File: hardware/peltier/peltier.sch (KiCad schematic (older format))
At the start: 33 parts, among them J1 Conn_01x02, J2 Conn_01x04, J3 Conn_01x04, J5 Conn_01x02, J6 Conn_01x03, Q1 IRF9Z34NPBF, Q2 IRF9Z34NPBF, Q3 IRFZ24NPBF, Q4 IRFZ24NPBF, U1 TC4420CPA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

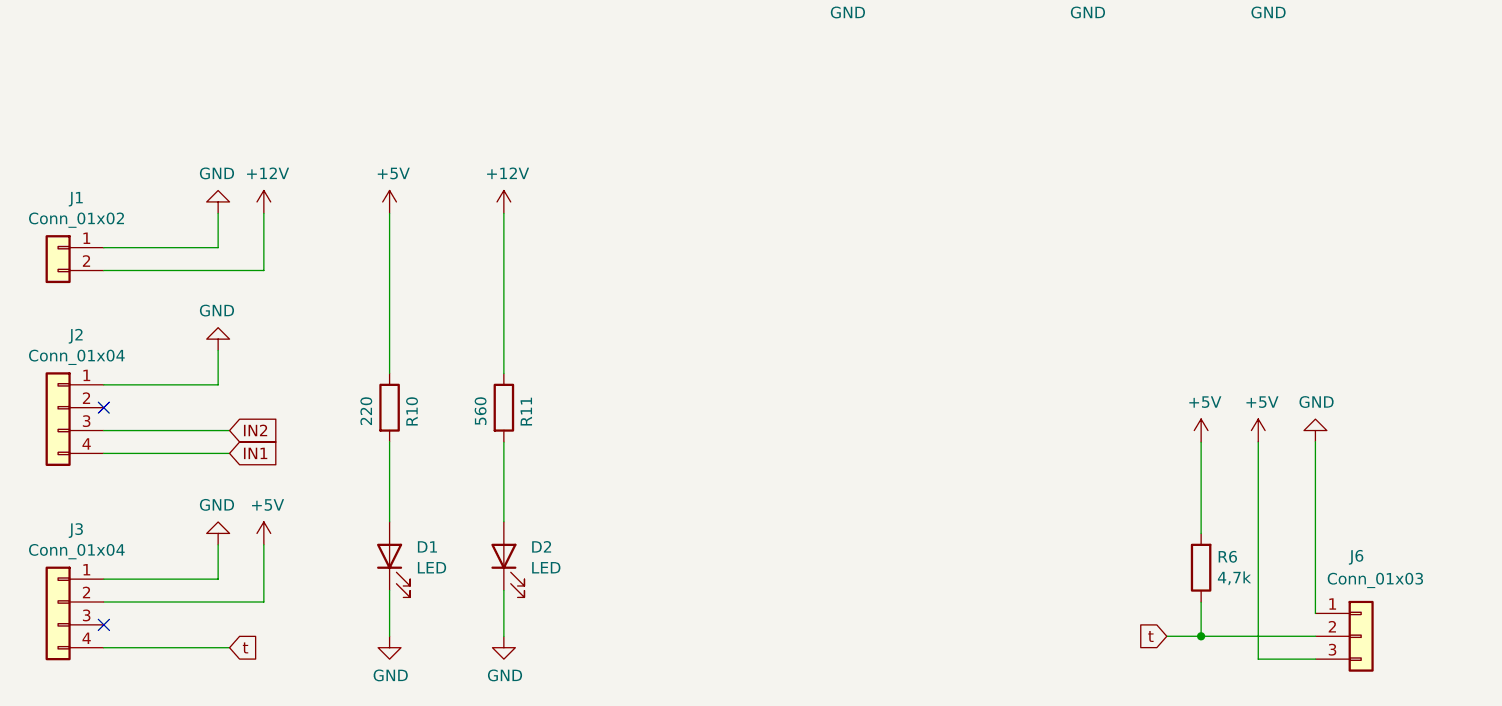
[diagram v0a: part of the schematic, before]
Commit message: Quick pinout fix for Peltier driver
Simple fix with  pinout now being correct
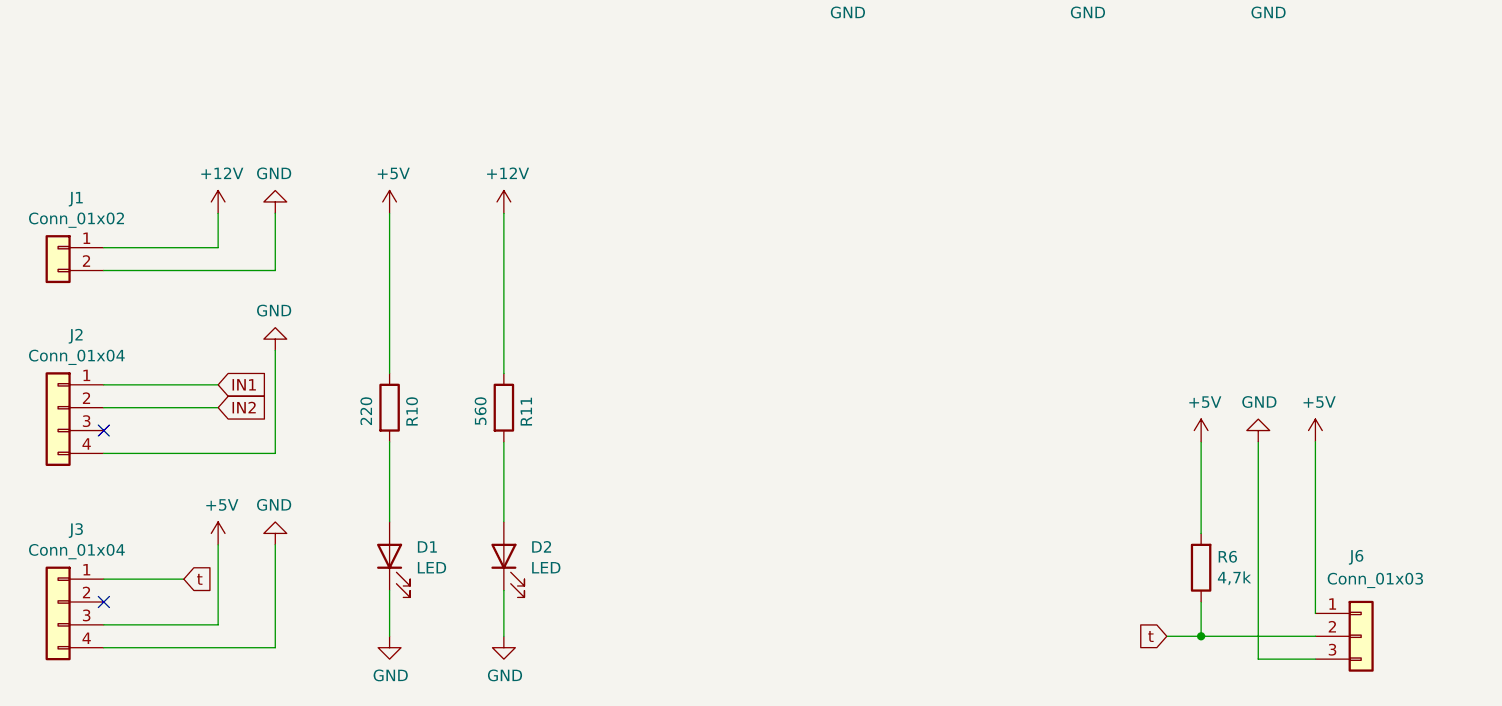
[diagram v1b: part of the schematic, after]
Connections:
- net +12V: now also J1.1 (Pin_1); no longer J1.2 (Pin_2)
- net +5V: now also J3.3 (Pin_3), J6.1 (Pin_1); no longer J3.2 (Pin_2), J6.3 (Pin_3)
- net GND: now also J1.2 (Pin_2), J2.4 (Pin_4), J3.4 (Pin_4), J6.3 (Pin_3); no longer J1.1 (Pin_1), J2.1 (Pin_1), J3.1 (Pin_1), J6.1 (Pin_1)
- net IN1: now also J2.1 (Pin_1); no longer J2.4 (Pin_4)
- net IN2: now also J2.2 (Pin_2); no longer J2.3 (Pin_3)
- net t: now also J3.1 (Pin_1); no longer J3.4 (Pin_4)
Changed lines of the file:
@@
 EESchema Schematic File Version 4
-LIBS:peltier-cache
 EELAYER 30 0
 EELAYER END
@@
 L power:GND #PWR022
 U 1 1 5F5A30FB
-P 6250 6650
-F 0 "#PWR022" H 6250 6400 50  0001 C CNN
-F 1 "GND" H 6255 6477 50  0000 C CNN
-F 2 "" H 6250 6650 50  0001 C CNN
-F 3 "" H 6250 6650 50  0001 C CNN
-	1    6250 6650
+P 6000 6650
+F 0 "#PWR022" H 6000 6400 50  0001 C CNN
+F 1 "GND" H 6005 6477 50  0000 C CNN
+F 2 "" H 6000 6650 50  0001 C CNN
+F 3 "" H 6000 6650 50  0001 C CNN
+	1    6000 6650
 	1    0    0    1
 $EndComp
@@
 L power:+5V #PWR021
 U 1 1 5F5B6024
-P 6000 6650
-F 0 "#PWR021" H 6000 6500 50  0001 C CNN
-F 1 "+5V" H 6015 6823 50  0000 C CNN
-F 2 "" H 6000 6650 50  0001 C CNN
-F 3 "" H 6000 6650 50  0001 C CNN
-	1    6000 6650
+P 6250 6650
+F 0 "#PWR021" H 6250 6500 50  0001 C CNN
+F 1 "+5V" H 6265 6823 50  0000 C CNN
+F 2 "" H 6250 6650 50  0001 C CNN
+F 3 "" H 6250 6650 50  0001 C CNN
+	1    6250 6650
 	1    0    0    -1
 $EndComp
@@
 L power:GND #PWR03
 U 1 1 5F58F426
-P 1450 6250
-F 0 "#PWR03" H 1450 6000 50  0001 C CNN
-F 1 "GND" H 1455 6077 50  0000 C CNN
-F 2 "" H 1450 6250 50  0001 C CNN
-F 3 "" H 1450 6250 50  0001 C CNN
-	1    1450 6250
+P 1700 6250
+F 0 "#PWR03" H 1700 6000 50  0001 C CNN
+F 1 "GND" H 1705 6077 50  0000 C CNN
+F 2 "" H 1700 6250 50  0001 C CNN
+F 3 "" H 1700 6250 50  0001 C CNN
+	1    1700 6250
 	-1   0    0    1
 $EndComp
@@
 L power:+5V #PWR08
 U 1 1 5F591312
-P 1650 7100
-F 0 "#PWR08" H 1650 6950 50  0001 C CNN
-F 1 "+5V" H 1665 7273 50  0000 C CNN
-F 2 "" H 1650 7100 50  0001 C CNN
-F 3 "" H 1650 7100 50  0001 C CNN
-	1    1650 7100
-	1    0    0    -1
-$EndComp
-Wire Wire Line
-	1500 6600 950  6600
+P 1450 7100
+F 0 "#PWR08" H 1450 6950 50  0001 C CNN
+F 1 "+5V" H 1465 7273 50  0000 C CNN
+F 2 "" H 1450 7100 50  0001 C CNN
+F 3 "" H 1450 7100 50  0001 C CNN
+	1    1450 7100
+	1    0    0    -1
+$EndComp
 $Comp
 L Connector_Generic:Conn_01x04 J3
@@
 L power:GND #PWR06
 U 1 1 5F59FAE5
-P 1450 7100
-F 0 "#PWR06" H 1450 6850 50  0001 C CNN
-F 1 "GND" H 1455 6927 50  0000 C CNN
-F 2 "" H 1450 7100 50  0001 C CNN
-F 3 "" H 1450 7100 50  0001 C CNN
-	1    1450 7100
+P 1700 7100
+F 0 "#PWR06" H 1700 6850 50  0001 C CNN
+F 1 "GND" H 1705 6927 50  0000 C CNN
+F 2 "" H 1700 7100 50  0001 C CNN
+F 3 "" H 1700 7100 50  0001 C CNN
+	1    1700 7100
 	-1   0    0    1
-$EndComp
-Wire Wire Line
-	1450 6400 1450 6250
-Wire Wire Line
-	1650 7100 1650 7350
-$Comp
-L Connector_Generic:Conn_01x02 J1
-U 1 1 5F5E0D51
-P 750 5800
-F 0 "J1" H 668 6017 50  0000 C CNN
-F 1 "Conn_01x02" H 668 5926 50  0000 C CNN
-F 2 "Connector_JST:JST_XH_B2B-XH-A_1x02_P2.50mm_Vertical" H 750 5800 50  0001 C CNN
-F 3 "~" H 750 5800 50  0001 C CNN
-	1    750  5800
-	-1   0    0    -1
 $EndComp
 $Comp
 L power:GND #PWR01
 U 1 1 5F5E28D2
+P 1700 5650
+F 0 "#PWR01" H 1700 5400 50  0001 C CNN
+F 1 "GND" H 1705 5477 50  0000 C CNN
+F 2 "" H 1700 5650 50  0001 C CNN
+F 3 "" H 1700 5650 50  0001 C CNN
+	1    1700 5650
+	-1   0    0    1
+$EndComp
+$Comp
+L power:+12V #PWR07
+U 1 1 5F5E4300
 P 1450 5650
-F 0 "#PWR01" H 1450 5400 50  0001 C CNN
-F 1 "GND" H 1455 5477 50  0000 C CNN
+F 0 "#PWR07" H 1450 5500 50  0001 C CNN
+F 1 "+12V" H 1465 5823 50  0000 C CNN
 F 2 "" H 1450 5650 50  0001 C CNN
 F 3 "" H 1450 5650 50  0001 C CNN
 	1    1450 5650
-	-1   0    0    1
-$EndComp
-Wire Wire Line
-	950  5800 1450 5800
-Wire Wire Line
-	1450 5800 1450 5650
-$Comp
-L power:+12V #PWR07
-U 1 1 5F5E4300
-P 1650 5650
-F 0 "#PWR07" H 1650 5500 50  0001 C CNN
-F 1 "+12V" H 1665 5823 50  0000 C CNN
-F 2 "" H 1650 5650 50  0001 C CNN
-F 3 "" H 1650 5650 50  0001 C CNN
-	1    1650 5650
-	1    0    0    -1
-$EndComp
-Wire Wire Line
-	1650 5650 1650 5900
-Wire Wire Line
-	950  5900 1650 5900
-Text GLabel 1500 6600 2    50   Input ~ 0
+	1    0    0    -1
+$EndComp
+Wire Wire Line
+	1450 5650 1450 5800
+Text GLabel 1450 6500 2    50   Input ~ 0
 IN2
-Text GLabel 1500 6700 2    50   Input ~ 0
+Text GLabel 1450 6400 2    50   Input ~ 0
 IN1
-Wire Wire Line
-	950  6700 1500 6700
-Text GLabel 1500 7550 2    50   Input ~ 0
+Text GLabel 1300 7250 2    50   Input ~ 0
 t
-Wire Wire Line
-	950  7550 1500 7550
 $Comp
 L TC4420CPA:TC4420CPA U1
@@
 Wire Wire Line
 	7250 4350 7250 4600
-NoConn ~ 950  7450
 $Comp
 L Device:LED D1
@@
 $EndComp
 Wire Wire Line
-	950  7250 1450 7250
-Wire Wire Line
-	1450 7250 1450 7100
-Wire Wire Line
-	950  7350 1650 7350
-NoConn ~ 950  6500
+	1700 5650 1700 5900
+Wire Wire Line
+	950  5800 1450 5800
+Wire Wire Line
+	950  5900 1700 5900
+$Comp
+L Connector_Generic:Conn_01x02 J1
+U 1 1 5F5E0D51
+P 750 5800
+F 0 "J1" H 668 6017 50  0000 C CNN
+F 1 "Conn_01x02" H 668 5926 50  0000 C CNN
+F 2 "Connector_JST:JST_XH_B2B-XH-A_1x02_P2.50mm_Vertical" H 750 5800 50  0001 C CNN
+F 3 "~" H 750 5800 50  0001 C CNN
+	1    750  5800
+	-1   0    0    -1
+$EndComp
+Wire Wire Line
+	950  6500 1450 6500
+Wire Wire Line
+	950  6700 1700 6700
+Wire Wire Line
+	1700 6250 1700 6700
+NoConn ~ 950  6600
+Wire Wire Line
+	950  7450 1450 7450
+Wire Wire Line
+	1450 7100 1450 7450
+Wire Wire Line
+	1300 7250 950  7250
+Wire Wire Line
+	1700 7100 1700 7550
+Wire Wire Line
+	950  7550 1700 7550
+NoConn ~ 950  7350
 $EndSCHEMATC
